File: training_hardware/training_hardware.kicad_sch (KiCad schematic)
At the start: 0 parts

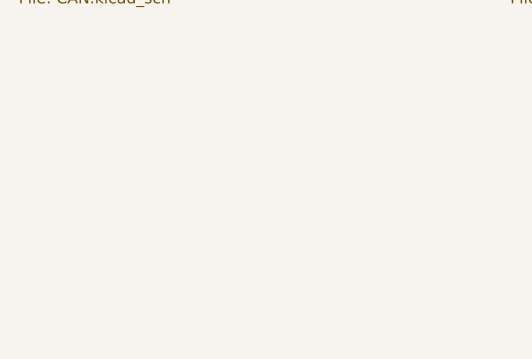
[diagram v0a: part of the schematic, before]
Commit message: Finished layout training
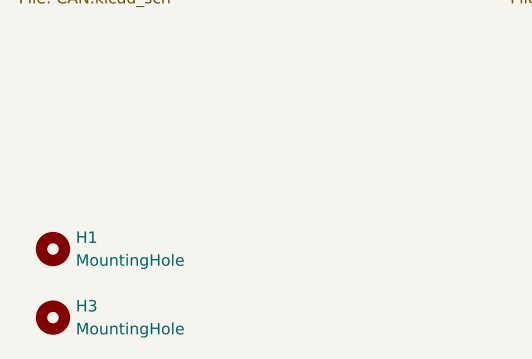
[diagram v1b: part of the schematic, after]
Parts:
- added H1, H3: MountingHole, MRDT_Drill_Holes:4_40_Hole_Corner, symbol Mechanical:MountingHole
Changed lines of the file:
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@@
+		)
+	)
+	(symbol
+		(lib_id "Mechanical:MountingHole")
+		(at 63.5 139.7 0)
+		(unit 1)
+		(exclude_from_sim no)
+		(in_bom no)
+		(on_board yes)
+		(dnp no)
+		(fields_autoplaced yes)
+		(property "Reference" "H3"
+			(at 66.04 138.4299 0)
+			(effects
+				(font
+					(size 1.27 1.27)
+				)
+				(justify left)
+			)
+		)
+		(property "Value" "MountingHole"
+			(at 66.04 140.9699 0)
+			(effects
+				(font
+					(size 1.27 1.27)
+				)
+				(justify left)
+			)
+		)
+		(property "Footprint" "MRDT_Drill_Holes:4_40_Hole_Corner"
+			(at 63.5 139.7 0)
+			(effects
+				(font
+					(size 1.27 1.27)
+				)
+				(hide yes)
+			)
+		)
+		(property "Datasheet" "~"
+			(at 63.5 139.7 0)
+			(effects
+				(font
+					(size 1.27 1.27)
+				)
+				(hide yes)
+			)
+		)
+		(property "Description" "Mounting Hole without connection"
+			(at 63.5 139.7 0)
+			(effects
+				(font
+					(size 1.27 1.27)
+				)
+				(hide yes)
+			)
+		)
+		(instances
+			(project "training_hardware"
+				(path "/19aa0e78-5ab4-46df-84c9-9ca161187559"
+					(reference "H3")
+					(unit 1)
+				)
+			)
+		)
+	)
+	(symbol
+		(lib_id "Mechanical:MountingHole")
+		(at 63.5 132.08 0)
+		(unit 1)
+		(exclude_from_sim no)
+		(in_bom no)
+		(on_board yes)
+		(dnp no)
+		(fields_autoplaced yes)
+		(property "Reference" "H1"
+			(at 66.04 130.8099 0)
+			(effects
+				(font
+					(size 1.27 1.27)
+				)
+				(justify left)
+			)
+		)
+		(property "Value" "MountingHole"
+			(at 66.04 133.3499 0)
+			(effects
+				(font
+					(size 1.27 1.27)
+				)
+				(justify left)
+			)
+		)
+		(property "Footprint" "MRDT_Drill_Holes:4_40_Hole_Corner"
+			(at 63.5 132.08 0)
+			(effects
+				(font
+					(size 1.27 1.27)
+				)
+				(hide yes)
+			)
+		)
+		(property "Datasheet" "~"
+			(at 63.5 132.08 0)
+			(effects
+				(font
+					(size 1.27 1.27)
+				)
+				(hide yes)
+			)
+		)
+		(property "Description" "Mounting Hole without connection"
+			(at 63.5 132.08 0)
+			(effects
+				(font
+					(size 1.27 1.27)
+				)
+				(hide yes)
+			)
+		)
+		(instances
+			(project ""
+				(path "/19aa0e78-5ab4-46df-84c9-9ca161187559"
+					(reference "H1")
+					(unit 1)
+				)
+			)
 		)
 	)
